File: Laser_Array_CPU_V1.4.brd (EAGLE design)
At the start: 104.1 x 109.6 mm, 72 parts, among them IC1 PIC24FJ64GA004, J1 MA16-2, J3 22-23-2021, J4 22-23-2021, J8 22-23-2021, J9 22-23-2021, U1 MAX6817, U2 LP2985-28DBVTE4, U4 LP2985-50DBVR, X1 22-23-2031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

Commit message: Finished Laser_Array next versions, all theee boards, Nov19_2018
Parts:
- removed D1, D2: S10M-TPMSCT_ND, Mine:S10M-TPMSCT-ND
- removed D4, D5: (no value), Mine:DO214AC
- removed J9: 22-23-2021, Mine:22-23-2021
- added C22: 1uF, rcl:C0805
- added C23: 4.7uF, rcl:C0805
- added U3: (no value), Mine:SOT223
- added X4: 22-23-2031, Mine:22-23-2031
- R3: value 10R, 5W -> 2R2, 5W
- moved X1 4.06 mm to (94.5, 101.0)
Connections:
- removed net N$33: D3.C, D4.A, R3.2
- net CHGA: now also X4.1; no longer J9.1
- net CHGB: now also X4.2; no longer J9.2
- net GND: now also C22.2, C23.2, U3.2, U3.4, X4.3
- net N$3: now also C22.1, U3.3; no longer D1.A, D2.C
- net N$37: no longer D5.A
- net VDD: no longer D4.C, D5.C
- net VDD_TB: now also C23.1, D3.C, R3.2, U3.1; no longer D2.A, D3.A, X2.1
- net VLASER: now also D3.A, X2.1; no longer D1.C
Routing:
- net N$33: track 26.6 -> 0.00 mm
- net VLASER: track 67.8 -> 82.1 mm
- net VDD_TB: track 19.8 -> 30.3 mm
- net VDD: track 278.7 -> 270.4 mm
- net N$37: track 16.5 -> 10.3 mm
- net CHGOUTA: track 102.4 -> 106.9 mm
- net CHGOUTB: track 101.3 -> 104.9 mm
- net N$3: track 6.14 -> 4.41 mm
- net CHGA: track 72.9 -> 74.2 mm
- net CHGB: track 72.5 -> 73.8 mm
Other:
- board text added: "Laser_Array_CPU, V1.4."
- board text added: "November 14, 1018 Terawatt Productions Inc."
- board text removed: "Laser_Array_CPU, V1.3."
- board text removed: "October 5, 1018 Terawatt Productions Inc."

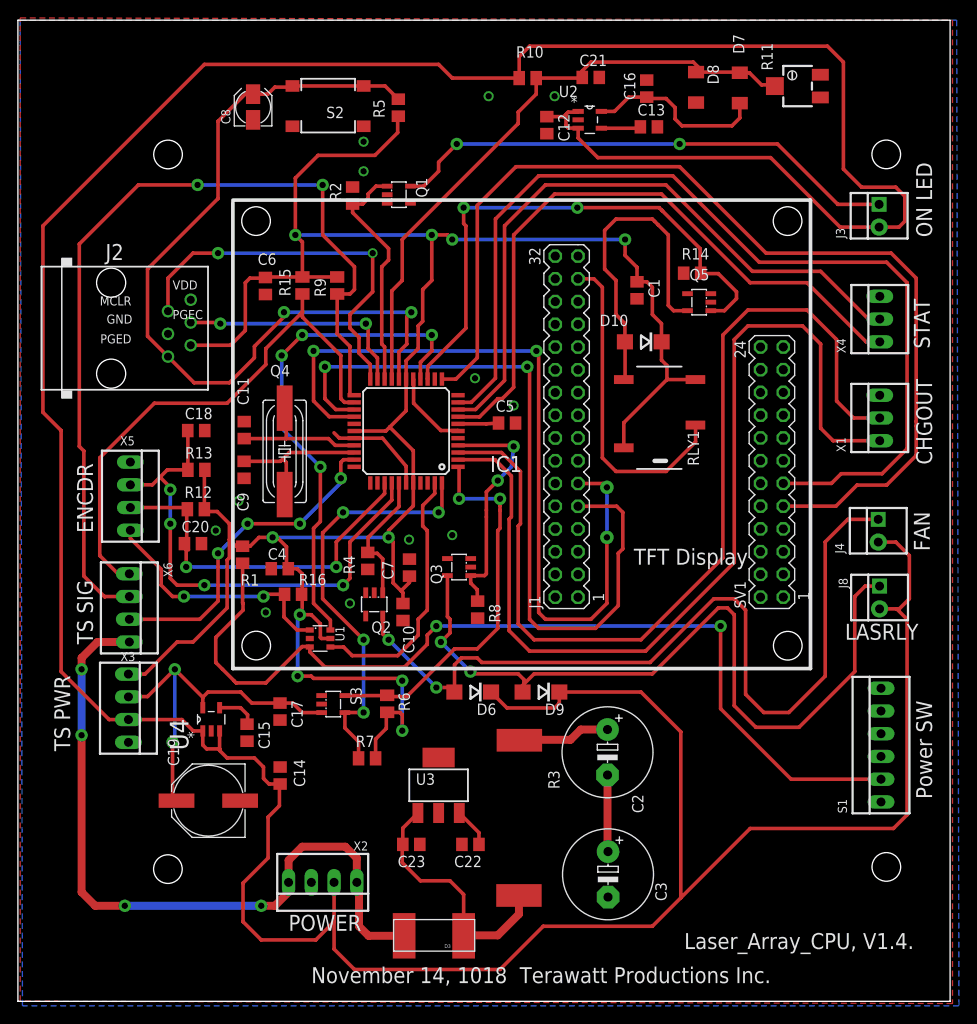
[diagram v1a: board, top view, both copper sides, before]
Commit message: Finished Laser_Array next versions, all three boards including revised charger board
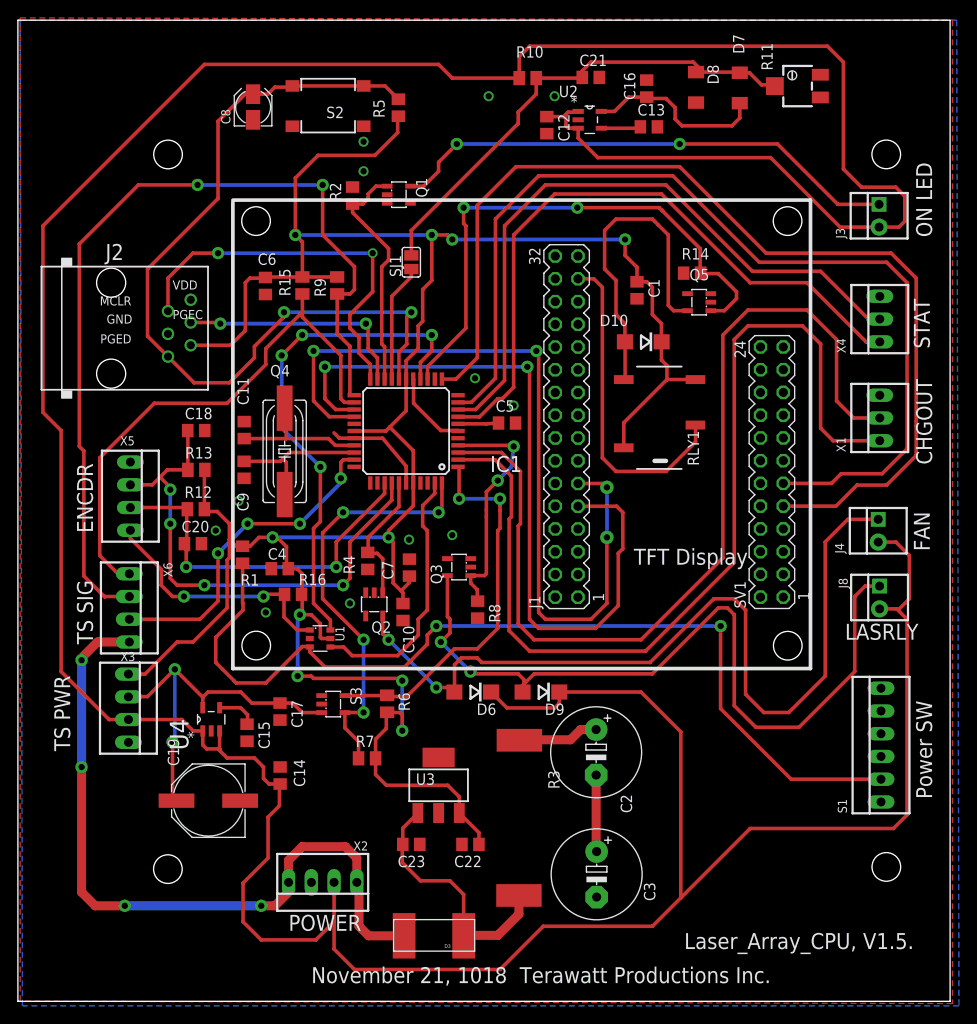
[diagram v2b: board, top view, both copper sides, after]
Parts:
- added SJ1: (no value), jumper:SJ
- moved C2 1.27 mm to (62.8, 63.6)
- moved C3 1.27 mm to (62.9, 50.0)
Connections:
- removed net N$3: C22.1, U3.3
- net VDD: now also C22.1, U3.3
- net VIN1: now also SJ1.1, SJ1.2
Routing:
- net VDD: track 270.4 -> 288.8 mm
- net N$3: track 4.41 -> 0.00 mm
- net VIN1: track 69.9 -> 68.4 mm
- net N$37: track 10.3 -> 9.07 mm
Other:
- board text added: "Laser_Array_CPU, V1.5."
- board text added: "November 21, 1018 Terawatt Productions Inc."
- board text removed: "Laser_Array_CPU, V1.4."
- board text removed: "November 14, 1018 Terawatt Productions Inc."

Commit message: Finished Laser_Array CPU Board V 1.5
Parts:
- R15, R9: value 4.7k -> 2.2k
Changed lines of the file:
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@@
 <attribute name="NAME" x="90.674" y="97.158" size="1.016" layer="25" ratio="10" rot="R90"/>
 </element>
-<element name="R9" library="rcl" package="M0805" value="4.7k" x="33.882" y="115.768" smashed="yes" rot="R90">
+<element name="R9" library="rcl" package="M0805" value="2.2k" x="33.882" y="115.768" smashed="yes" rot="R90">
 <attribute name="NAME" x="32.612" y="114.498" size="1.27" layer="25" rot="R90"/>
 </element>
-<element name="R15" library="rcl" package="M0805" value="4.7k" x="30" y="115.768" smashed="yes" rot="R90">
+<element name="R15" library="rcl" package="M0805" value="2.2k" x="30" y="115.768" smashed="yes" rot="R90">
 <attribute name="NAME" x="27.404" y="117.658" size="1.27" layer="25" rot="R270"/>
 </element>
